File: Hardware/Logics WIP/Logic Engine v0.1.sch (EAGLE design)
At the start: 32 parts, among them IC1 MEGA328P, Y1 16MHz

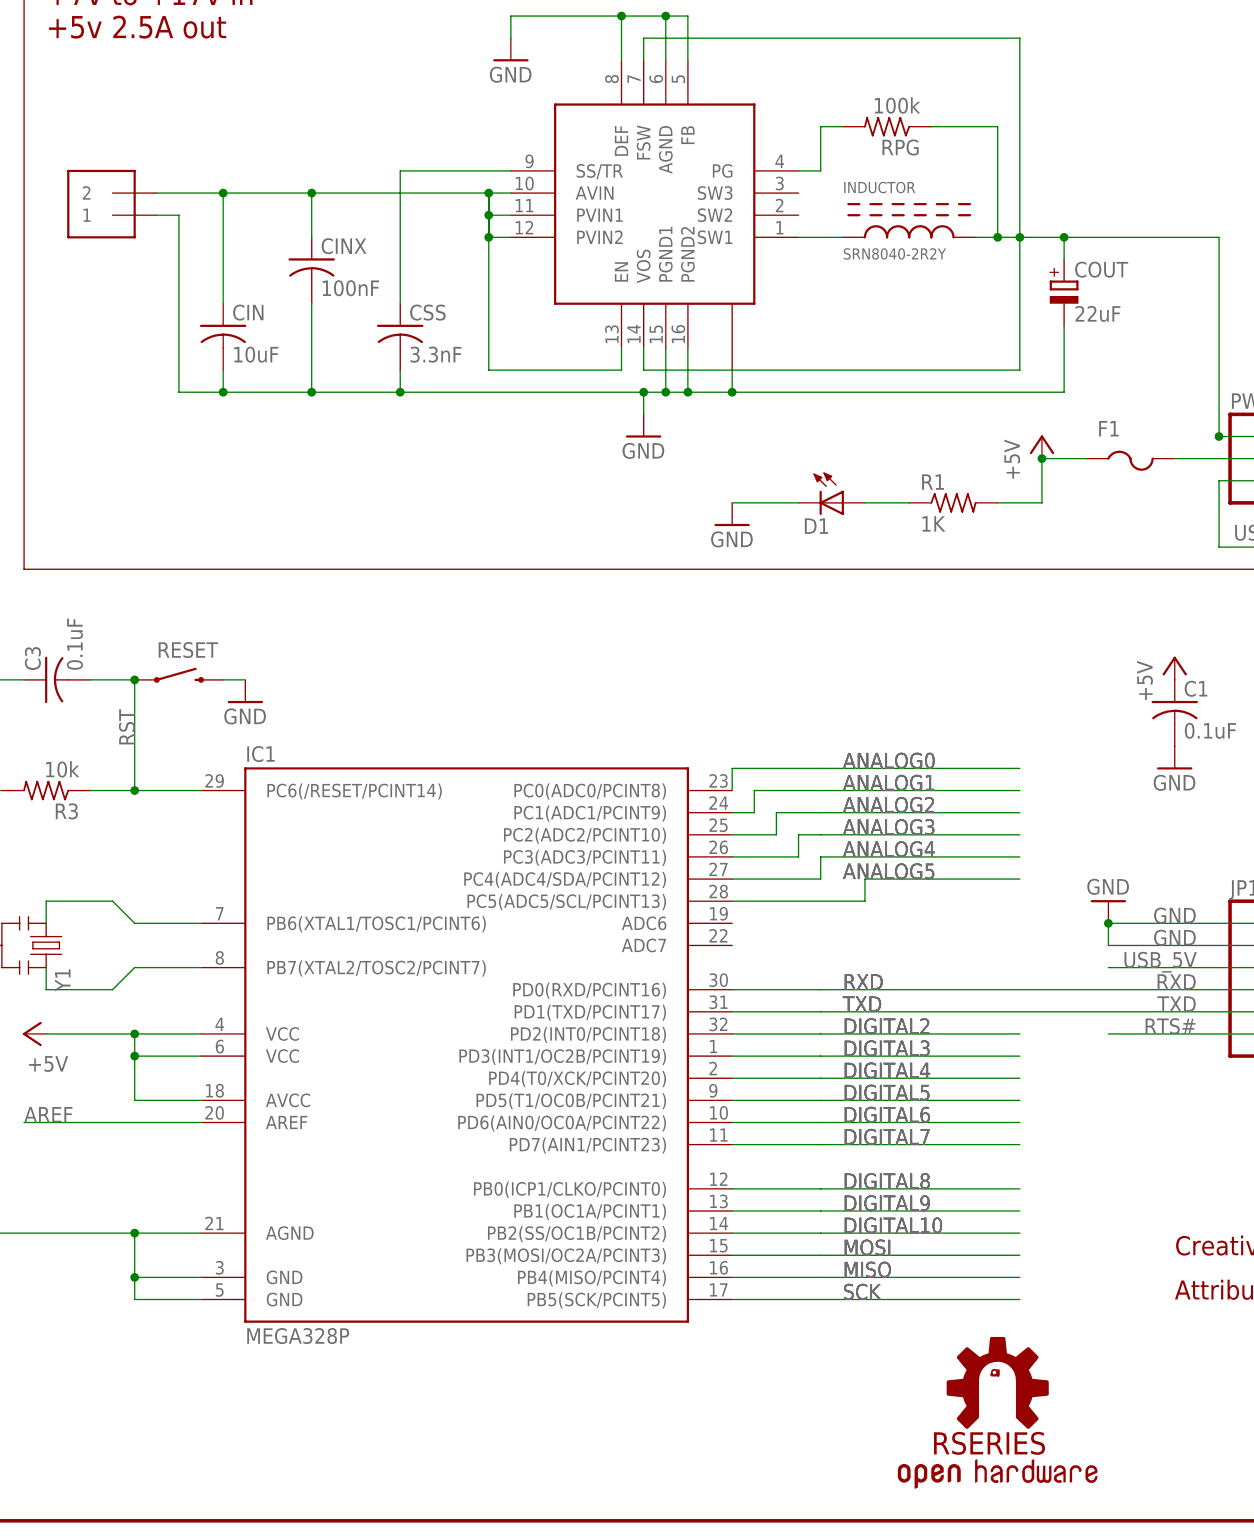
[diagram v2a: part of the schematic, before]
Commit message: 
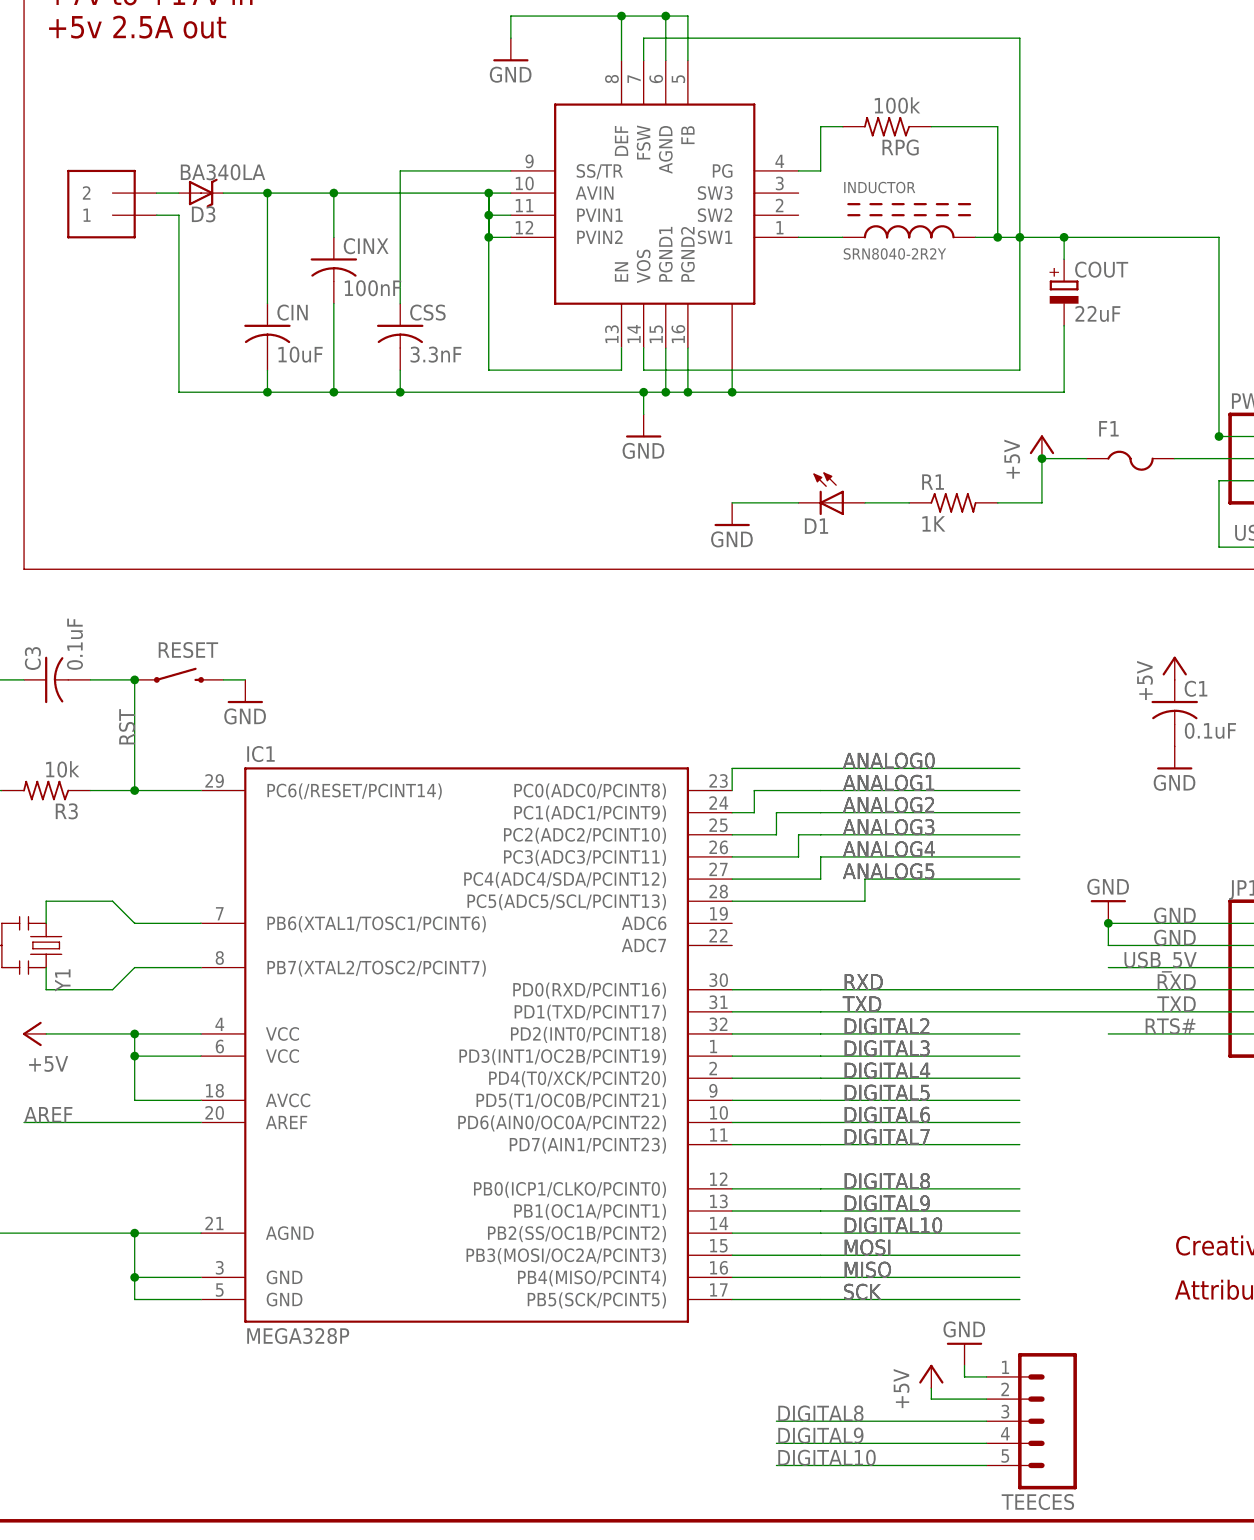
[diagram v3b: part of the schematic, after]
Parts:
- removed U$2: RSERIES-OSHW-LOGOMEDIUM, rseries:RSERIES-OSHW-LOGOMEDIUM
- added D3: BA340LA, SparkFun-DiscreteSemi:B340A
- added TEECES: (no value), SparkFun-Connectors:M05PTH
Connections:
- new net N$11: D3.A, EXT.PWR.2
- net +5V: now also TEECES.2
- net DIGITAL10: now also TEECES.5
- net DIGITAL8: now also TEECES.3
- net DIGITAL9: now also TEECES.4
- net GND: now also TEECES.1
- net N$6: now also D3.C; no longer EXT.PWR.2
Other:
- moved on the sheet: CIN, CINX
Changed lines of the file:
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@@
 <setting verticaltext="up"/>
 </settings>
-<grid distance="0.1" unitdist="inch" unit="inch" style="lines" multiple="1" display="no" altdistance="0.01" altunitdist="inch" altunit="inch"/>
+<grid distance="0.05" unitdist="inch" unit="inch" style="lines" multiple="1" display="no" altdistance="0.01" altunitdist="inch" altunit="inch"/>
 <layers>
 <layer number="1" name="Top" color="4" fill="1" visible="no" active="no"/>
@@
 <part name="P+11" library="supply1" deviceset="+5V" device=""/>
 <part name="GND18" library="supply1" deviceset="GND" device=""/>
-<part name="U$2" library="rseries" deviceset="RSERIES-OSHW-LOGO" device="MEDIUM"/>
 <part name="IC1" library="avr-7" deviceset="MEGA48/88/168" device="-AU" value="MEGA328P"/>
 <part name="P+13" library="supply1" deviceset="+5V" device=""/>
@@
 <part name="BRIGHT" library="rseries" deviceset="TRIMPOT" device="3364W"/>
 <part name="COLOR" library="rseries" deviceset="TRIMPOT" device="3364W"/>
+<part name="D3" library="SparkFun-DiscreteSemi" deviceset="B340A" device="" value="BA340LA"/>
+<part name="TEECES" library="SparkFun-Connectors" deviceset="M05" device="PTH"/>
+<part name="GND8" library="supply1" deviceset="GND" device=""/>
+<part name="P+8" library="supply1" deviceset="+5V" device=""/>
 </parts>
 <sheets>
@@
 <instance part="P+11" gate="1" x="180.34" y="129.54" rot="R180"/>
 <instance part="GND18" gate="1" x="198.12" y="160.02"/>
-<instance part="U$2" gate="G$1" x="129.54" y="5.08"/>
 <instance part="IC1" gate="1" x="71.12" y="55.88"/>
 <instance part="P+13" gate="1" x="20.32" y="55.88" rot="R90"/>
@@
 <instance part="P+7" gate="1" x="210.82" y="76.2" rot="R90"/>
 <instance part="REG" gate="G$1" x="83.82" y="149.86" rot="R180"/>
-<instance part="CINX" gate="G$1" x="53.34" y="144.78"/>
+<instance part="CINX" gate="G$1" x="55.88" y="144.78"/>
 <instance part="CSS" gate="G$1" x="63.5" y="137.16"/>
 <instance part="RPG" gate="G$1" x="119.38" y="160.02" rot="R180"/>
@@
 <instance part="R3" gate="G$1" x="22.86" y="83.82" rot="R180"/>
 <instance part="EXT.PWR" gate="G$1" x="30.48" y="152.4" rot="R180"/>
-<instance part="CIN" gate="G$1" x="43.18" y="137.16"/>
+<instance part="CIN" gate="G$1" x="48.26" y="137.16"/>
 <instance part="R1" gate="G$1" x="127" y="116.84"/>
 <instance part="R2" gate="G$1" x="231.14" y="53.34"/>
@@
 <attribute name="VALUE" x="232.41" y="72.39" size="1.778" layer="96" rot="R180"/>
 </instance>
+<instance part="D3" gate="G$1" x="40.64" y="152.4" smashed="yes">
+<attribute name="NAME" x="39.37" y="149.0726" size="1.778" layer="95"/>
+<attribute name="VALUE" x="38.1" y="153.8986" size="1.778" layer="96"/>
+</instance>
+<instance part="TEECES" gate="G$1" x="138.43" y="11.43" rot="R180"/>
+<instance part="GND8" gate="1" x="128.27" y="20.32" rot="MR180"/>
+<instance part="P+8" gate="1" x="124.46" y="17.78"/>
 </instances>
 <busses>
@@
 <segment>
 <wire x1="38.1" y1="149.86" x2="38.1" y2="129.54" width="0.1524" layer="91"/>
-<wire x1="38.1" y1="129.54" x2="43.18" y2="129.54" width="0.1524" layer="91"/>
-<wire x1="43.18" y1="129.54" x2="53.34" y2="129.54" width="0.1524" layer="91"/>
-<wire x1="53.34" y1="129.54" x2="63.5" y2="129.54" width="0.1524" layer="91"/>
+<wire x1="38.1" y1="129.54" x2="48.26" y2="129.54" width="0.1524" layer="91"/>
+<wire x1="48.26" y1="129.54" x2="55.88" y2="129.54" width="0.1524" layer="91"/>
+<wire x1="55.88" y1="129.54" x2="63.5" y2="129.54" width="0.1524" layer="91"/>
 <wire x1="63.5" y1="129.54" x2="91.44" y2="129.54" width="0.1524" layer="91"/>
 <wire x1="91.44" y1="129.54" x2="91.44" y2="127" width="0.1524" layer="91"/>
 <pinref part="GND19" gate="1" pin="GND"/>
-<wire x1="43.18" y1="132.08" x2="43.18" y2="129.54" width="0.1524" layer="91"/>
-<junction x="43.18" y="129.54"/>
+<wire x1="48.26" y1="132.08" x2="48.26" y2="129.54" width="0.1524" layer="91"/>
+<junction x="48.26" y="129.54"/>
 <pinref part="CINX" gate="G$1" pin="2"/>
-<wire x1="53.34" y1="139.7" x2="53.34" y2="129.54" width="0.1524" layer="91"/>
-<junction x="53.34" y="129.54"/>
+<wire x1="55.88" y1="139.7" x2="55.88" y2="129.54" width="0.1524" layer="91"/>
+<junction x="55.88" y="129.54"/>
 <pinref part="CSS" gate="G$1" pin="2"/>
 <wire x1="63.5" y1="132.08" x2="63.5" y2="129.54" width="0.1524" layer="91"/>
@@
 <pinref part="C1" gate="G$1" pin="2"/>
 </segment>
+<segment>
+<pinref part="TEECES" gate="G$1" pin="1"/>
+<pinref part="GND8" gate="1" pin="GND"/>
+<wire x1="130.81" y1="16.51" x2="128.27" y2="16.51" width="0.1524" layer="91"/>
+<wire x1="128.27" y1="16.51" x2="128.27" y2="17.78" width="0.1524" layer="91"/>
+</segment>
 </net>
 <net name="N$1" class="0">
@@
 <pinref part="C1" gate="G$1" pin="1"/>
 </segment>
+<segment>
+<pinref part="TEECES" gate="G$1" pin="2"/>
+<pinref part="P+8" gate="1" pin="+5V"/>
+<wire x1="130.81" y1="13.97" x2="124.46" y2="13.97" width="0.1524" layer="91"/>
+<wire x1="124.46" y1="13.97" x2="124.46" y2="15.24" width="0.1524" layer="91"/>
+</segment>
 </net>
 <net name="MOSI" class="0">
@@
 <wire x1="101.6" y1="33.02" x2="111.76" y2="33.02" width="0.1524" layer="91"/>
 </segment>
+<segment>
+<wire x1="130.81" y1="6.35" x2="106.68" y2="6.35" width="0.1524" layer="91"/>
+<label x="106.68" y="6.35" size="1.778" layer="95"/>
+<pinref part="TEECES" gate="G$1" pin="5"/>
+</segment>
 </net>
 <net name="DIGITAL9" class="0">
@@
 <wire x1="111.76" y1="35.56" x2="101.6" y2="35.56" width="0.1524" layer="91"/>
 </segment>
+<segment>
+<pinref part="TEECES" gate="G$1" pin="4"/>
+<wire x1="130.81" y1="8.89" x2="106.68" y2="8.89" width="0.1524" layer="91"/>
+<label x="106.68" y="8.89" size="1.778" layer="95"/>
+</segment>
 </net>
 <net name="DIGITAL8" class="0">
@@
 <wire x1="101.6" y1="38.1" x2="111.76" y2="38.1" width="0.1524" layer="91"/>
 </segment>
+<segment>
+<wire x1="130.81" y1="11.43" x2="106.68" y2="11.43" width="0.1524" layer="91"/>
+<label x="106.68" y="11.43" size="1.778" layer="95"/>
+<pinref part="TEECES" gate="G$1" pin="3"/>
+</segment>
 </net>
 <net name="DIGITAL7" class="0">
@@
 <net name="N$6" class="1">
 <segment>
-<wire x1="43.18" y1="139.7" x2="43.18" y2="152.4" width="0.1524" layer="91"/>
-<wire x1="43.18" y1="152.4" x2="53.34" y2="152.4" width="0.1524" layer="91"/>
+<wire x1="48.26" y1="139.7" x2="48.26" y2="152.4" width="0.1524" layer="91"/>
+<wire x1="48.26" y1="152.4" x2="55.88" y2="152.4" width="0.1524" layer="91"/>
 <pinref part="CINX" gate="G$1" pin="1"/>
-<junction x="53.34" y="152.4"/>
-<wire x1="53.34" y1="147.32" x2="53.34" y2="152.4" width="0.1524" layer="91"/>
-<wire x1="53.34" y1="152.4" x2="73.66" y2="152.4" width="0.1524" layer="91"/>
+<junction x="55.88" y="152.4"/>
+<wire x1="55.88" y1="147.32" x2="55.88" y2="152.4" width="0.1524" layer="91"/>
+<wire x1="55.88" y1="152.4" x2="73.66" y2="152.4" width="0.1524" layer="91"/>
 <pinref part="REG" gate="G$1" pin="PVIN1"/>
 <wire x1="76.2" y1="149.86" x2="73.66" y2="149.86" width="0.1524" layer="91"/>
@@
 <wire x1="76.2" y1="147.32" x2="73.66" y2="147.32" width="0.1524" layer="91"/>
 <junction x="73.66" y="147.32"/>
-<pinref part="EXT.PWR" gate="G$1" pin="2"/>
-<wire x1="35.56" y1="152.4" x2="43.18" y2="152.4" width="0.1524" layer="91"/>
-<junction x="43.18" y="152.4"/>
 <pinref part="CIN" gate="G$1" pin="1"/>
+<pinref part="D3" gate="G$1" pin="C"/>
+<wire x1="43.18" y1="152.4" x2="48.26" y2="152.4" width="0.1524" layer="91"/>
+<junction x="48.26" y="152.4"/>
 </segment>
 </net>
@@
 </segment>
 </net>
+<net name="N$11" class="0">
+<segment>
+<pinref part="EXT.PWR" gate="G$1" pin="2"/>
+<pinref part="D3" gate="G$1" pin="A"/>
+<wire x1="35.56" y1="152.4" x2="38.1" y2="152.4" width="0.1524" layer="91"/>
+</segment>
+</net>
